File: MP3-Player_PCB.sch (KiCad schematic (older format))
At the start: 25 parts, among them J1 USB_B_Micro, J2 Conn_01x02, J3 Micro_SD_Card, Q1 DMG2301L, SW1 SW_SPDT, U1 MCP73831-2-OT, U2 LM1117-3.3

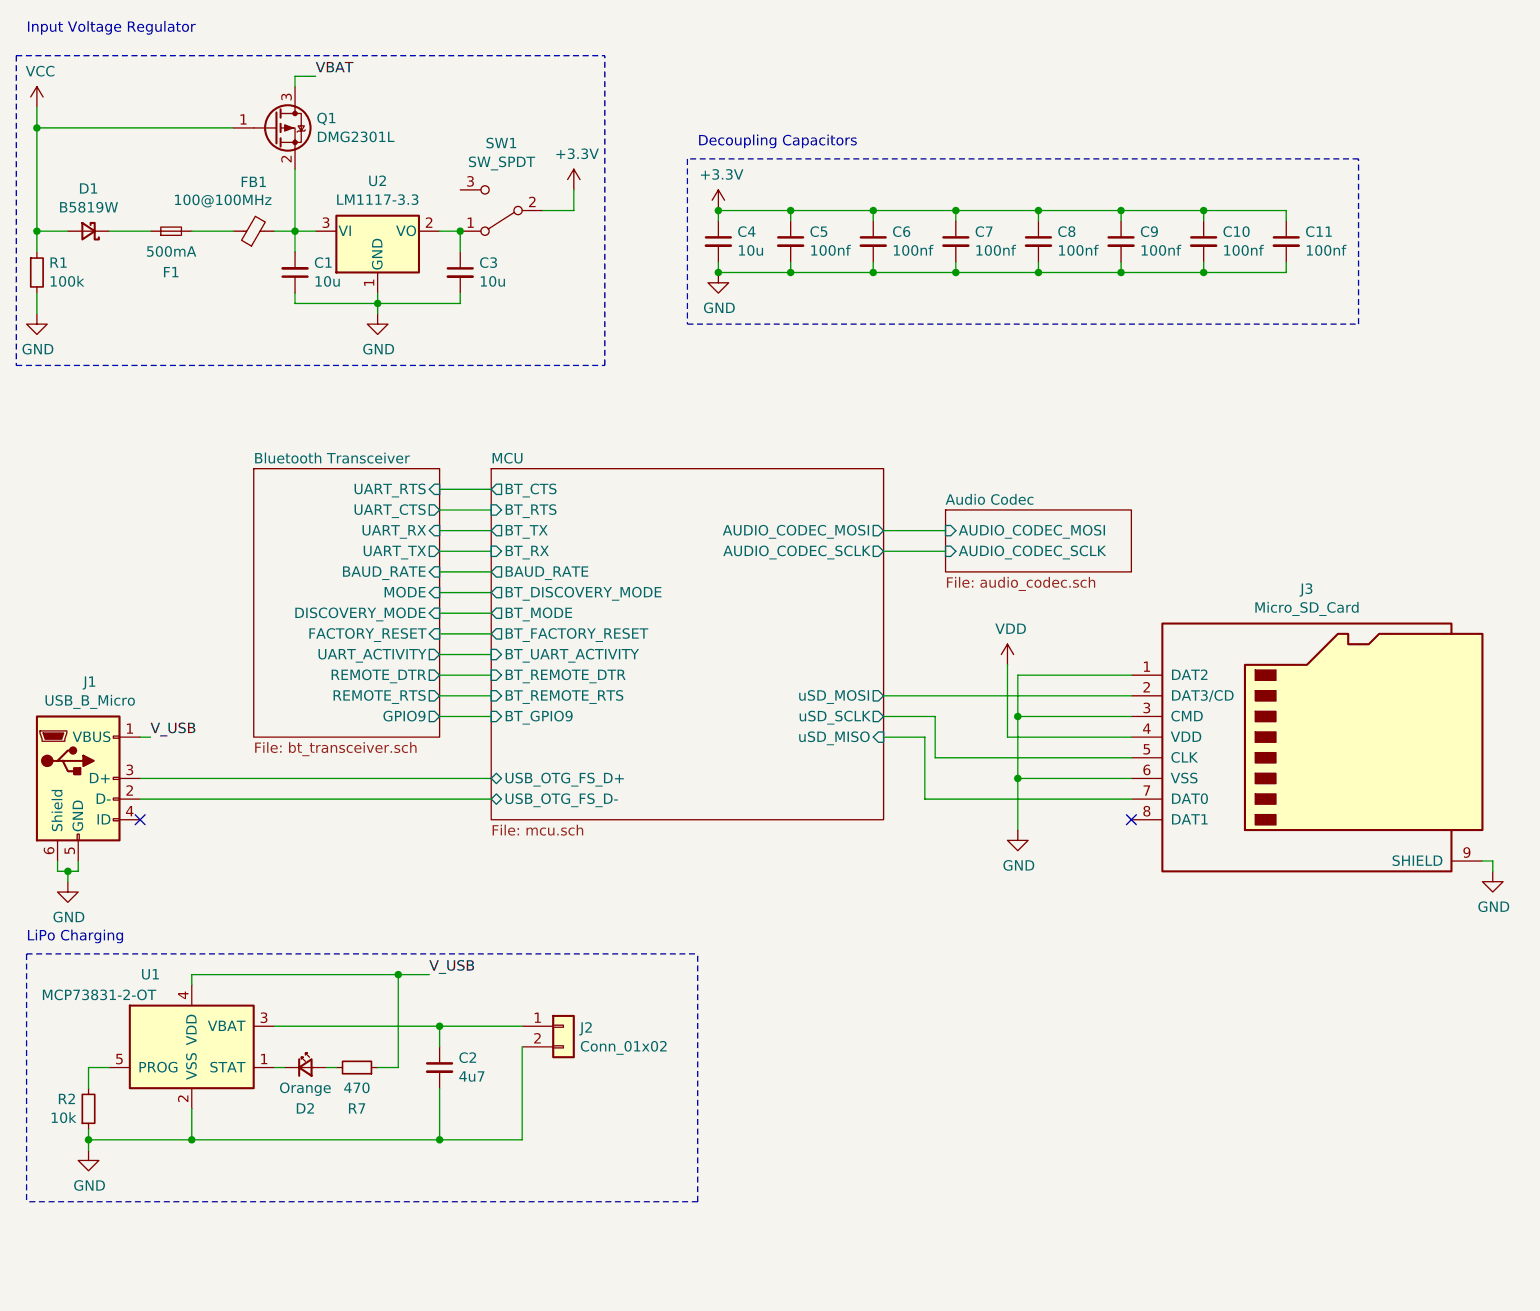
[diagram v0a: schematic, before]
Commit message: Updated the MCU
Updated the MCU to one that is on JLCPCB so that I can get it ordered from JLCPCB.
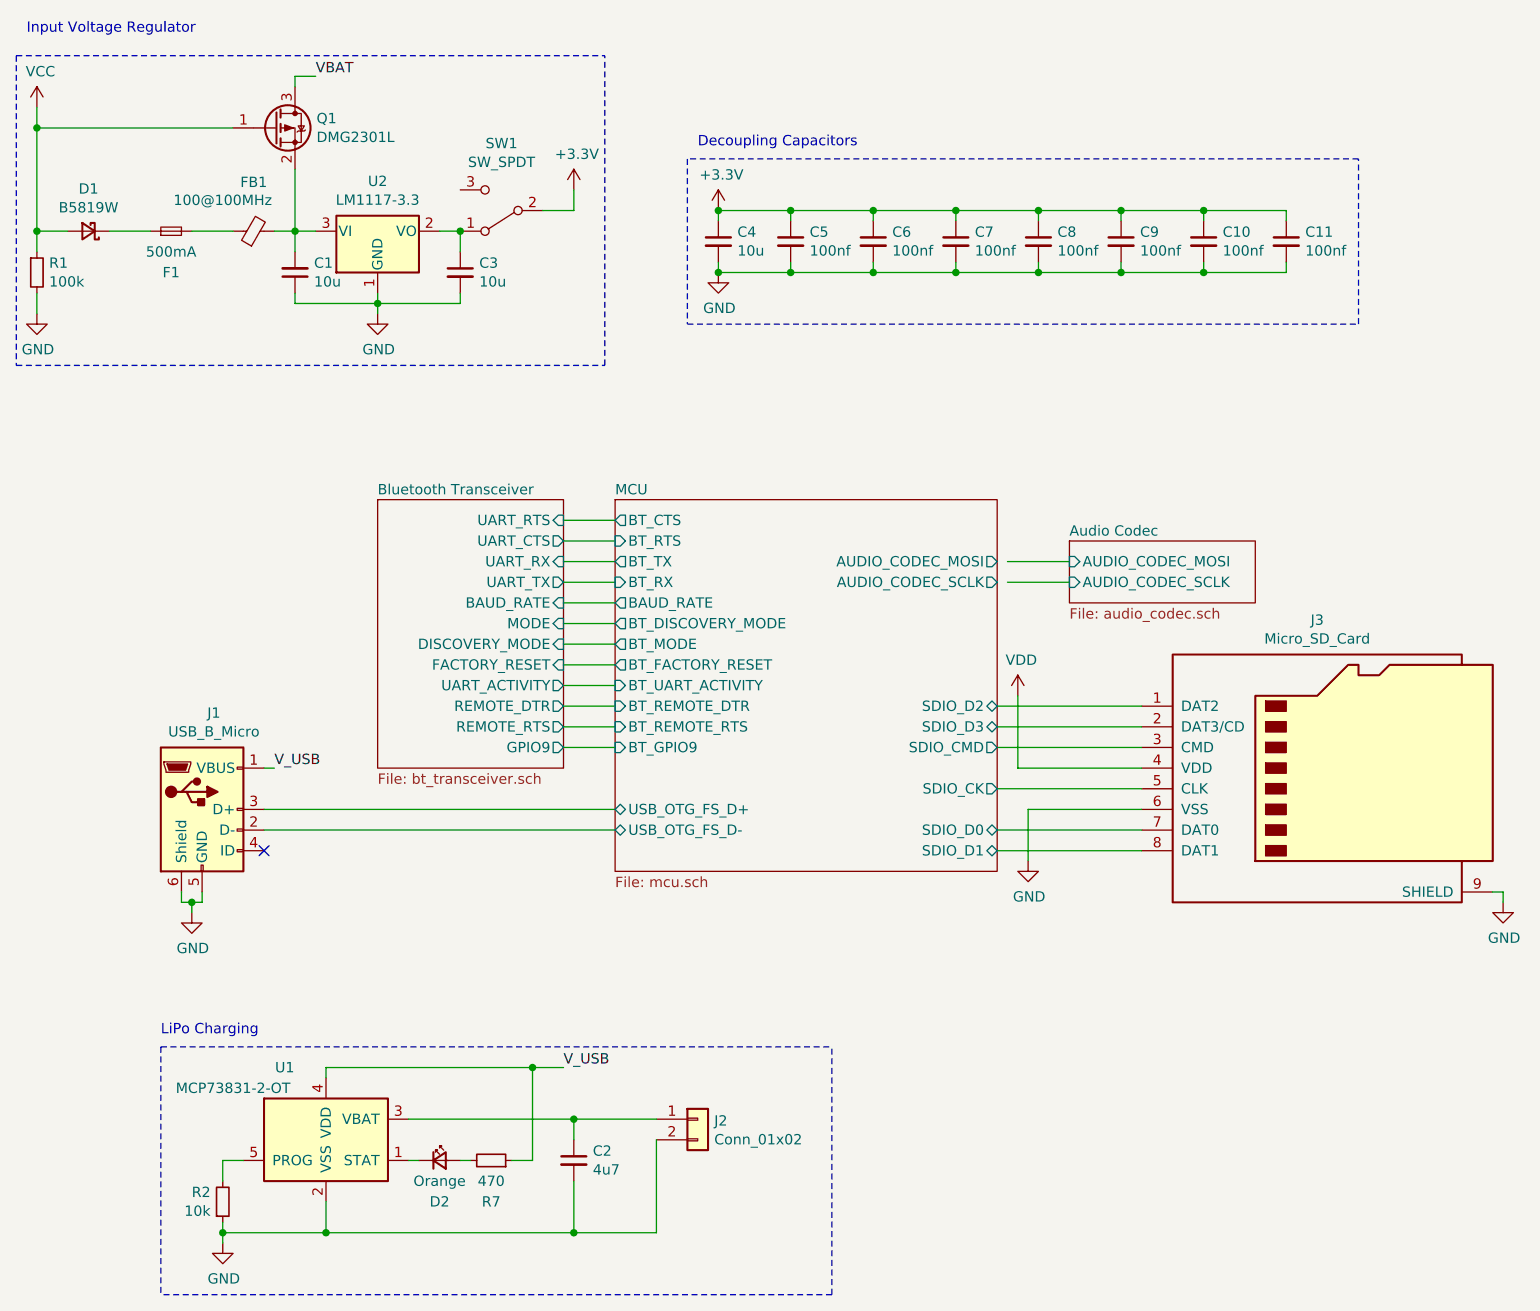
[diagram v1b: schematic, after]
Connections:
- net GND: no longer J3.1 (DAT2), J3.3 (CMD)
- net MCU/SDIO_D1: now reaches J3.8 (DAT1)
- net MCU/uSD_MISO renamed MCU/SDIO_D0
- net MCU/uSD_MOSI renamed MCU/SDIO_D3
- net MCU/uSD_SCLK renamed MCU/SDIO_CK
- new net MCU/SDIO_CMD: J3.3 (CMD)
- new net MCU/SDIO_D2: J3.1 (DAT2)
- no-connect marks 2 -> 1
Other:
- moved on the sheet: C2, D2, J1, J2, J3, R2, R7, U1

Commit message: Updated footprints
Updated some parts to JLCPCB SMT library and also added some footprints
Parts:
- C1: footprint (none) -> Capacitor_SMD:C_0805_2012Metric
- C10, C11, C5, C6, C7, C8, C9: value 100nf -> 100n; footprint (none) -> Capacitor_SMD:C_0402_1005Metric
- C2: renamed from C3; footprint (none) -> Capacitor_SMD:C_0805_2012Metric
- C3: renamed from C4; footprint (none) -> Capacitor_SMD:C_0805_2012Metric
- C4: renamed from C2; footprint (none) -> Capacitor_SMD:C_0805_2012Metric
- D1: footprint (none) -> Diode_SMD:D_SOD-123
- D2: footprint (none) -> LED_SMD:LED_0805_2012Metric
- F1: footprint (none) -> Fuse:Fuse_1206_3216Metric
- J1: footprint (none) -> Connector_USB:USB_Micro-B_Amphenol_10103594-0001LF_Horizontal
- J3: footprint (none) -> Connector_Card:microSD_HC_Molex_104031-0811
- renumbered R7 to R3, U2 to U1, U1 to U2
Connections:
- net VCC is gone; now on net V_USB: D1.2 (A), Q1.1 (G), R1.1
- net VDD is gone; now on net +3V3: J3.4 (VDD)
- net VBAT: now also C4.1, J2.1 (Pin_1), U2.3 (VBAT)
- no-connect marks 1 -> 2
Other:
- moved on the sheet: C1, C10, C11, C2, C3, C4, C5, C6, C7, C8, C9, D1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

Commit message: Update footprints
Add footprints for resistors, push buttons, regulator, and crystals
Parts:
- FB1: footprint (none) -> Ferrite_THT:LairdTech_28C0236-0JW-10
- J2: footprint (none) -> Connector_Molex:Molex_CLIK-Mate_502382-0270_1x02-1MP_P1.25mm_Vertical
- R1, R2: footprint (none) -> Resistor_SMD:R_1206_3216Metric
- R3: footprint (none) -> Resistor_SMD:R_0805_2012Metric
- SW1: footprint (none) -> Button_Switch_THT:SW_Slide_1P2T_CK_OS102011MS2Q
- U1: footprint (none) -> Diode_SMD:D_SMB_Modified
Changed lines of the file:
@@
 F 0 "FB1" V 4137 2000 50  0000 C CNN
 F 1 "100@100MHz" V 4050 2150 50  0000 C CNN
-F 2 "" V 3830 2000 50  0001 C CNN
+F 2 "Ferrite_THT:LairdTech_28C0236-0JW-10" V 3830 2000 50  0001 C CNN
 F 3 "~" H 3900 2000 50  0001 C CNN
 	1    3900 2000
@@
 F 0 "R2" H 3641 6454 50  0000 R CNN
 F 1 "10k" H 3641 6545 50  0000 R CNN
-F 2 "" H 3700 6500 50  0001 C CNN
+F 2 "Resistor_SMD:R_1206_3216Metric" H 3700 6500 50  0001 C CNN
 F 3 "~" H 3700 6500 50  0001 C CNN
 	1    3700 6500
@@
 F 0 "J2" H 8230 5892 50  0000 L CNN
 F 1 "Conn_01x02" H 8230 5801 50  0000 L CNN
-F 2 "" H 8150 5900 50  0001 C CNN
+F 2 "Connector_Molex:Molex_CLIK-Mate_502382-0270_1x02-1MP_P1.25mm_Vertical" H 8150 5900 50  0001 C CNN
 F 3 "~" H 8150 5900 50  0001 C CNN
 	1    8150 5900
@@
 F 0 "R1" H 2909 2246 50  0000 L CNN
 F 1 "100k" H 2909 2155 50  0000 L CNN
-F 2 "" H 2850 2200 50  0001 C CNN
+F 2 "Resistor_SMD:R_1206_3216Metric" H 2850 2200 50  0001 C CNN
 F 3 "~" H 2850 2200 50  0001 C CNN
 	1    2850 2200
@@
 F 0 "U1" H 4500 2242 50  0000 C CNN
 F 1 "LM1117-3.3" H 4500 2151 50  0000 C CNN
-F 2 "" H 4500 2000 50  0001 C CNN
+F 2 "Diode_SMD:D_SMB_Modified" H 4500 2000 50  0001 C CNN
 F 3 "http://www.ti.com/lit/ds/symlink/lm1117.pdf" H 4500 2000 50  0001 C CNN
 	1    4500 2000
@@
 F 0 "R3" V 4800 6300 50  0000 C CNN
 F 1 "470" V 4900 6300 50  0000 C CNN
-F 2 "" H 5000 6300 50  0001 C CNN
+F 2 "Resistor_SMD:R_0805_2012Metric" H 5000 6300 50  0001 C CNN
 F 3 "~" H 5000 6300 50  0001 C CNN
 	1    5000 6300
@@
 F 0 "SW1" H 5100 1575 50  0000 C CNN
 F 1 "SW_SPDT" H 5100 1666 50  0000 C CNN
-F 2 "" H 5100 1900 50  0001 C CNN
+F 2 "Button_Switch_THT:SW_Slide_1P2T_CK_OS102011MS2Q" H 5100 1900 50  0001 C CNN
 F 3 "~" H 5100 1900 50  0001 C CNN
 	1    5100 1900

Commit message: Updating parts
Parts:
- added BT1: Battery_Cell, symbol Device:Battery_Cell
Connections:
- net GND: now also BT1.2 (-)
- net VBAT: now also BT1.1 (+)
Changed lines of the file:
@@
 Wire Wire Line
 	6700 3650 7050 3650
+$Comp
+L Device:Battery_Cell BT1
+U 1 1 6144A74D
+P 6550 6000
+F 0 "BT1" H 6668 6096 50  0000 L CNN
+F 1 "Battery_Cell" H 6668 6005 50  0000 L CNN
+F 2 "" V 6550 6060 50  0001 C CNN
+F 3 "~" V 6550 6060 50  0001 C CNN
+	1    6550 6000
+	1    0    0    -1
+$EndComp
+Wire Wire Line
+	6650 5700 6550 5700
+Wire Wire Line
+	6550 5700 6550 5800
+Text Label 6650 5700 0    50   ~ 0
+VBAT
+$Comp
+L power:GND #PWR0102
+U 1 1 6144F2C7
+P 6550 6200
+F 0 "#PWR0102" H 6550 5950 50  0001 C CNN
+F 1 "GND" H 6555 6027 50  0000 C CNN
+F 2 "" H 6550 6200 50  0001 C CNN
+F 3 "" H 6550 6200 50  0001 C CNN
+	1    6550 6200
+	1    0    0    -1
+$EndComp
+Wire Wire Line
+	6550 6200 6550 6100
 $EndSCHEMATC
